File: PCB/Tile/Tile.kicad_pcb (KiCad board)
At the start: 2 copper layers, 100 x 100 mm, 95 parts, among them J1 Conn_01x04_Male, J2 Conn_01x04, J3 Conn_01x02_Male, U1 HT16K33-28SOP

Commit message: [add] Tileの回路図を作成 #3
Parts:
- removed C2: 100u, Capacitor_THT:CP_Radial_D5.0mm_P2.50mm
- removed J2: Conn_01x04, Connector:NS-Tech_Grove_1x04_P2mm_Vertical
- removed J3: Conn_01x02_Male, Connector_PinHeader_2.54mm:PinHeader_1x02_P2.54mm_Vertical
- removed JP4, JP5: Jumper_NO_Small, Jumper:SolderJumper-2_P1.3mm_Open_RoundedPad1.0x1.5mm
- removed LS1: Speaker, extsui:Speaker_UGSM23A
- removed R4, R5: 4.7k, extsui:R_1608_HandSolderingCustom
- removed TP1, TP10, TP11, TP12, TP13, TP14, TP15, TP16, TP2, TP3, TP4, TP5, TP6, TP7, TP8, TP9: TestPoint, extsui:TestPoint_Pad_2.0x2.0mm_NoSilk
- added H1: MountingHole, MountingHole:MountingHole_3.2mm_M3, F.Cu at (125.5, 185.5)
- added H2: MountingHole, MountingHole:MountingHole_3.2mm_M3, F.Cu at (125.5, 192.4)
- added H3: MountingHole, MountingHole:MountingHole_3.2mm_M3, F.Cu at (132.4, 185.5)
- added H4: MountingHole, MountingHole:MountingHole_3.2mm_M3, F.Cu at (132.4, 192.4)
- added H5: MountingHole, MountingHole:MountingHole_3.2mm_M3, F.Cu at (139.4, 185.5)
- added H6: MountingHole, MountingHole:MountingHole_3.2mm_M3, F.Cu at (139.4, 192.4)
- J1: value Conn_01x04_Male -> Conn_01x05_Female; footprint Connector_PinHeader_2.54mm:PinHeader_1x04_P2.54mm_Vertical -> Connector_PinHeader_2.54mm:PinHeader_1x05_P2.54mm_Vertical
- moved J1 8.54 mm to (115.0, 63.0), turned to 0 degrees
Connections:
- C1 pad 1: VCC -> +5V
- D9 pad 2: Net-(D25-Pad2) -> Net-(D9-Pad2)
- J1 pad 1: SCL -> +5V
- J1 pad 3: VCC -> SCL
- J1 pad 4: GND -> Net-(J1-Pad4)
- U1 pad 17: Net-(D25-Pad2) -> Net-(D9-Pad2)
- U1 pad 28: VCC -> +5V
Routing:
- net SDA: track 286.8 -> 184.0 mm, vias 9 -> 6
- net VCC: track 232.4 -> 130.2 mm, vias 9 -> 7
- net SCL: track 240.3 -> 153.1 mm, vias 11 -> 8
- net Net-(J3-Pad1): track 31.1 -> 0.00 mm
- net Net-(J3-Pad2): track 29.8 -> 0.00 mm
- net GND: track 13.1 -> 0.00 mm, vias 7 -> 4
- net Net-(JP5-Pad1): track 4.91 -> 0.00 mm
- net Net-(JP4-Pad1): track 4.91 -> 0.00 mm
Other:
- outline, holes or cut-outs redrawn
- board text added: "@ext_sui 2020.04"
- board text added: "Tile Growing v1.0"
- board text removed: "@ext_sui 2019.03"
- board text removed: "Land Growing v1.0"

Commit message: [update] TileのLED仮位置決め完了 #3
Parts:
- removed D25: LED, extsui:LED_1608_HandSolderingCustom
- removed REF1, REF2, REF3, REF4: MountingHole_3.2mm_M3, MountingHole:MountingHole_3.2mm_M3
- removed TP17, TP18, TP19, TP20, TP21, TP22, TP23, TP24, TP25, TP26, TP27, TP28, TP29, TP30, TP31, TP32, TP33, TP34, TP35, TP36, TP37, TP38, TP39, TP40, TP41, TP42, TP43, TP44, TP45, TP46, TP47, TP48: TestPoint, extsui:TestPoint_Pad_2.0x2.0mm_NoSilk
- moved H4 126.9 mm to (152.0, 67.0)
- moved H5 122.6 mm to (108.0, 67.0)
- moved H6 102.4 mm to (86.0, 105.0)
- moved H3 90.6 mm to (174.0, 105.0)
- moved D19 82.4 mm to (97.0, 91.9), turned to 60 degrees
- moved D18 78.3 mm to (102.0, 83.2), turned to 60 degrees
- moved D17 73.2 mm to (107.0, 74.5), turned to 60 degrees
- moved D20 73.1 mm to (92.0, 100.5), turned to 60 degrees
- moved D1 71.1 mm to (115.0, 140.0)
- moved D7 70.8 mm to (162.5, 118.2), turned to 60 degrees
- moved D8 69.0 mm to (167.5, 109.5), turned to 60 degrees
- moved D9 67.7 mm to (167.5, 100.5), turned to 300 degrees
- moved D10 66.7 mm to (162.5, 91.8), turned to 300 degrees
- moved D16 63.6 mm to (115.0, 70.0), turned to 0 degrees
- moved D6 63.3 mm to (157.5, 126.8), turned to 60 degrees
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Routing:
- net Net-(D1-Pad1): track 214.7 -> 0.00 mm, vias 6 -> 0
- net SDA: track 184.0 -> 0.00 mm, vias 6 -> 0
- net SCL: track 153.1 -> 0.00 mm, vias 8 -> 0
- net Net-(D17-Pad1): track 152.1 -> 0.00 mm, vias 1 -> 0
- net Net-(D23-Pad2): track 145.9 -> 0.00 mm, vias 2 -> 0
- net Net-(D22-Pad2): track 141.0 -> 0.00 mm, vias 2 -> 0
- net Net-(D24-Pad2): track 130.5 -> 0.00 mm, vias 4 -> 0
- net VCC: track 130.2 -> 0.00 mm, vias 7 -> 0
- net Net-(D21-Pad2): track 124.8 -> 0.00 mm, vias 2 -> 0
- net Net-(D25-Pad2): track 112.4 -> 0.00 mm, vias 4 -> 0
- net Net-(D20-Pad2): track 107.0 -> 0.00 mm, vias 2 -> 0
- net Net-(D19-Pad2): track 96.1 -> 0.00 mm, vias 2 -> 0
- net Net-(D18-Pad2): track 90.2 -> 0.09 mm, vias 2 -> 0
- net Net-(D10-Pad2): track 72.1 -> 0.00 mm, vias 1 -> 0
- net Net-(D12-Pad2): track 69.2 -> 0.00 mm, vias 3 -> 0
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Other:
- board size 100 x 100 mm -> 100 x 86.6 mm
- board text removed: "GND"
- board text removed: "SCL"
- board text removed: "SDA"
- board text removed: "VCC"

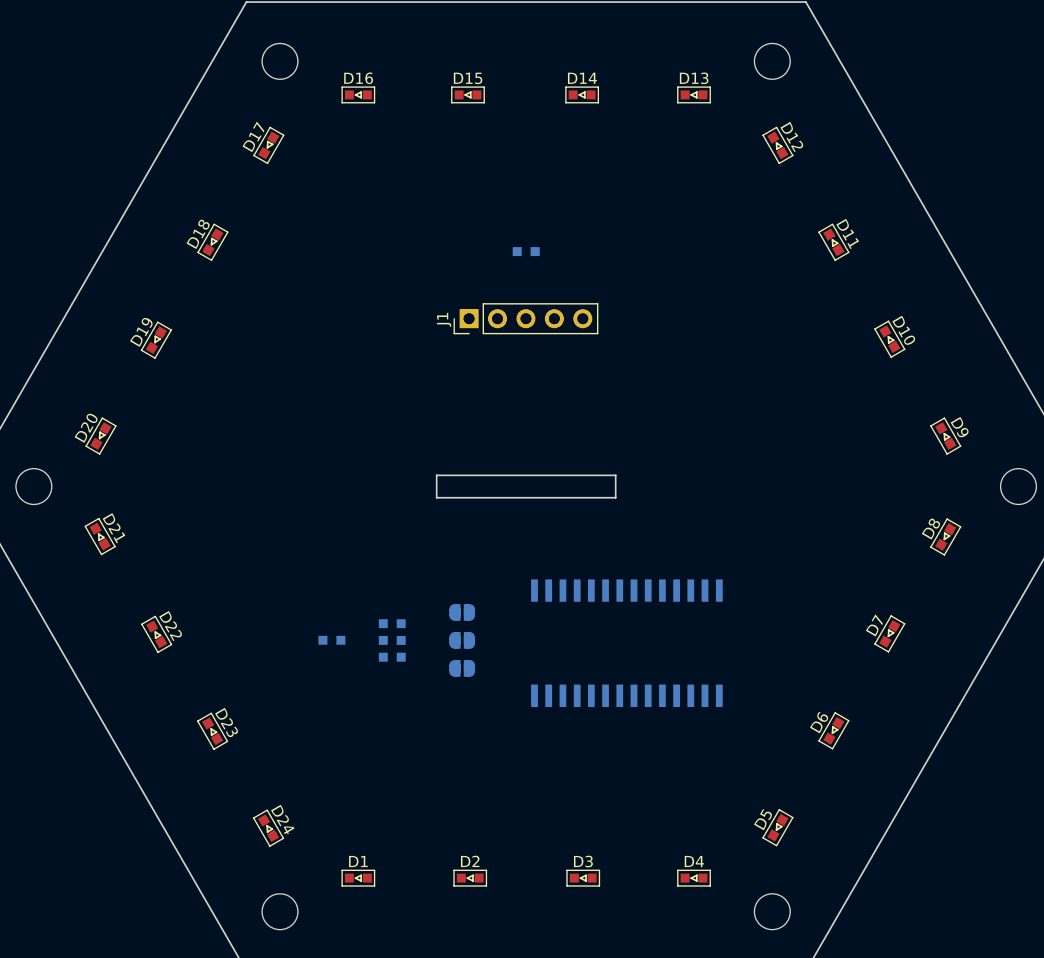
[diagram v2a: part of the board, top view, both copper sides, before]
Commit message: [update] TileのLED外周配線作成 #3
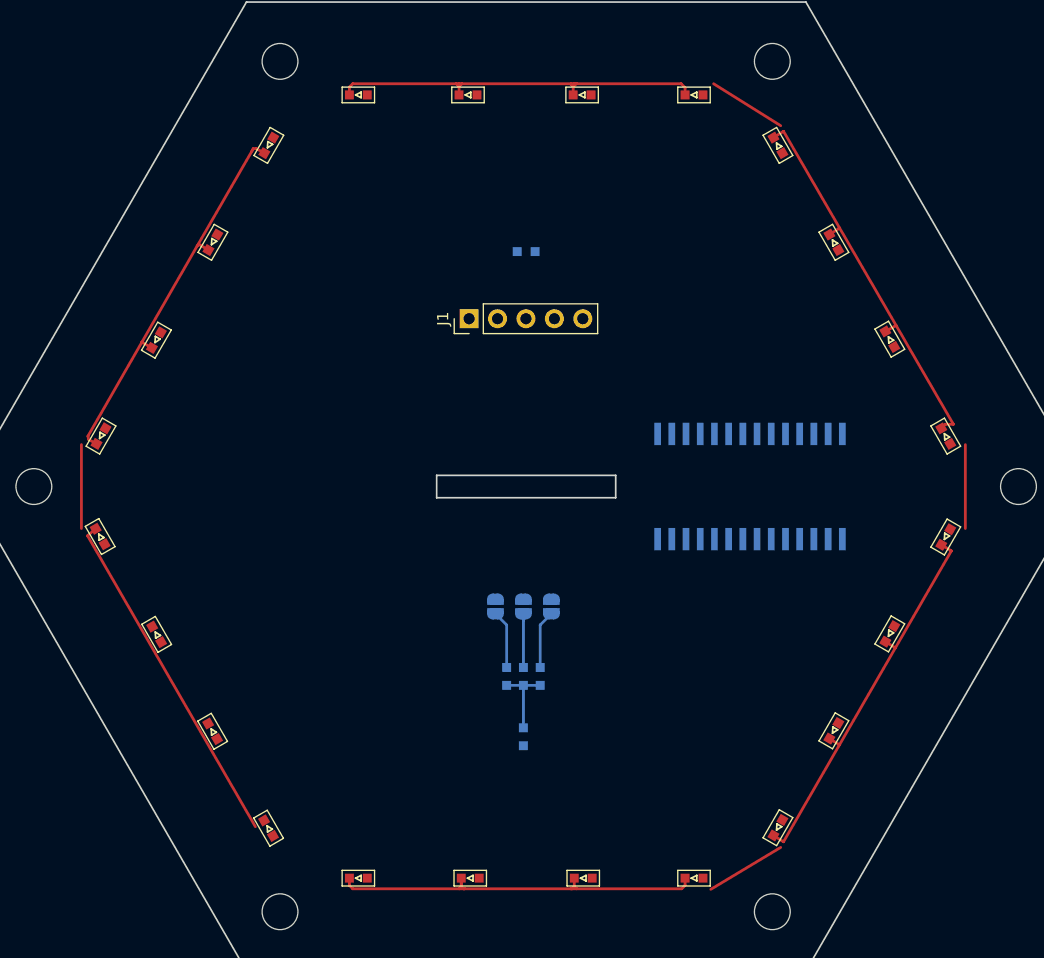
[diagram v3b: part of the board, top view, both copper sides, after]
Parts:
- moved D26 19.2 mm to (129.7, 127.4), turned to 270 degrees
- moved U1 17.8 mm to (150.0, 105.0)
- moved R1 13.3 mm to (131.3, 122.0), turned to 270 degrees
- moved R2 12.2 mm to (129.8, 122.0), turned to 270 degrees
- moved R3 11.3 mm to (128.3, 122.0), turned to 270 degrees
- moved JP1 9.71 mm to (132.3, 115.7), turned to 90 degrees
- moved JP2 6.26 mm to (129.8, 115.7), turned to 90 degrees
- moved JP3 3.02 mm to (127.3, 115.7), turned to 90 degrees
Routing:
- net Net-(D1-Pad1): track 0.00 -> 161.0 mm
- net Net-(D17-Pad1): track 0.00 -> 72.4 mm
- net Net-(D26-Pad1): track 0.01 -> 6.79 mm
- net Net-(JP3-Pad1): track 0.00 -> 5.21 mm
- net Net-(JP1-Pad1): track 0.00 -> 5.21 mm
- net Net-(JP2-Pad1): track 0.00 -> 4.80 mm

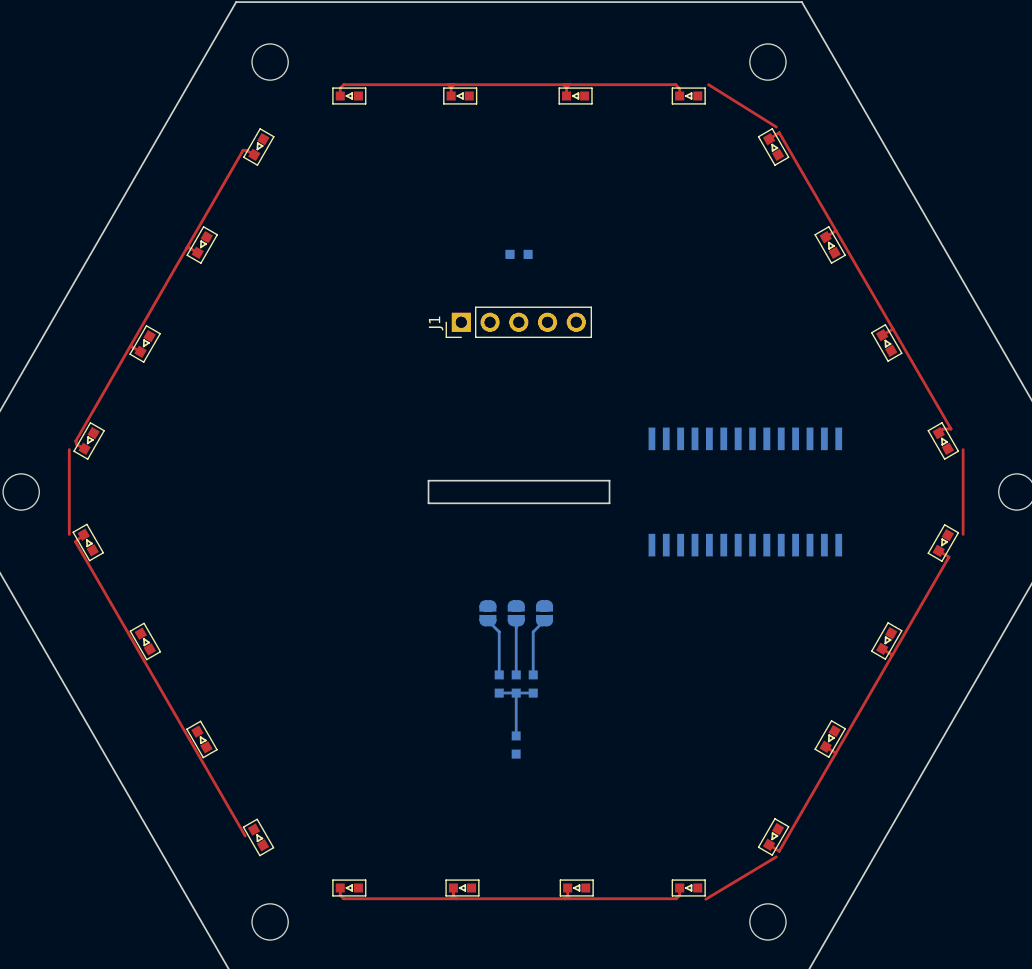
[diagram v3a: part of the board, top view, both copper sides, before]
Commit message: [update] TileのLED並び替え後の位置決め完了 #3
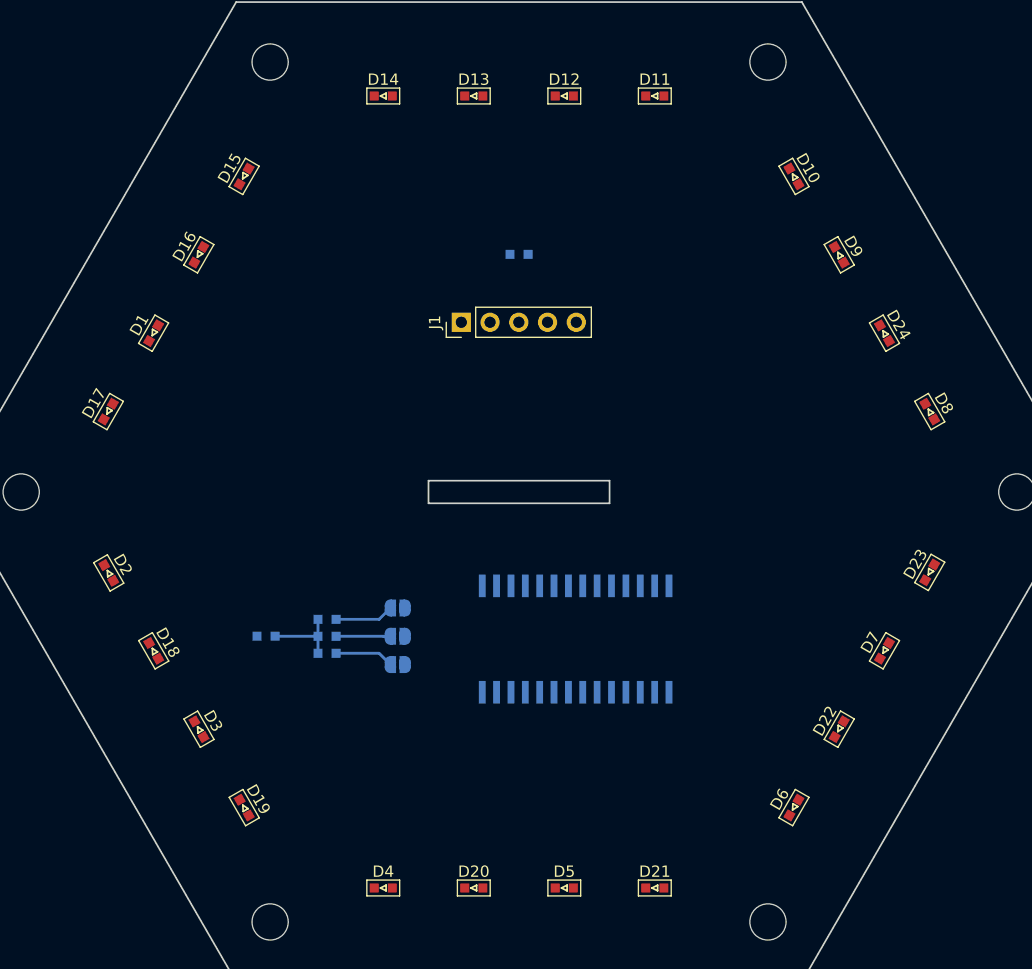
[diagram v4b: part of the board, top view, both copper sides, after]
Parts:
- moved D24 71.0 mm to (162.3, 91.0)
- moved D23 66.0 mm to (166.3, 112.1), turned to 60 degrees
- moved D22 61.8 mm to (158.3, 126.0), turned to 60 degrees
- moved D21 58.6 mm to (142.0, 140.0), turned to 0 degrees
- moved D20 52.1 mm to (126.0, 140.0), turned to 0 degrees
- moved D1 52.0 mm to (97.7, 91.0), turned to 60 degrees
- moved D19 41.9 mm to (105.7, 132.9), turned to 300 degrees
- moved D2 41.9 mm to (93.7, 112.2), turned to 300 degrees
- moved D3 36.2 mm to (101.7, 126.0), turned to 300 degrees
- moved D18 36.1 mm to (97.7, 119.0), turned to 300 degrees
- moved D4 27.0 mm to (118.0, 140.0)
- moved D17 26.9 mm to (93.7, 97.9)
- moved D26 24.1 mm to (107.6, 117.7), turned to 180 degrees
- moved D15 20.4 mm to (105.7, 77.1), turned to 60 degrees
- moved D11 20.3 mm to (142.0, 70.0), turned to 0 degrees
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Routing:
- net Net-(D1-Pad1): track 161.0 -> 0.00 mm
- net Net-(D17-Pad1): track 72.4 -> 0.00 mm

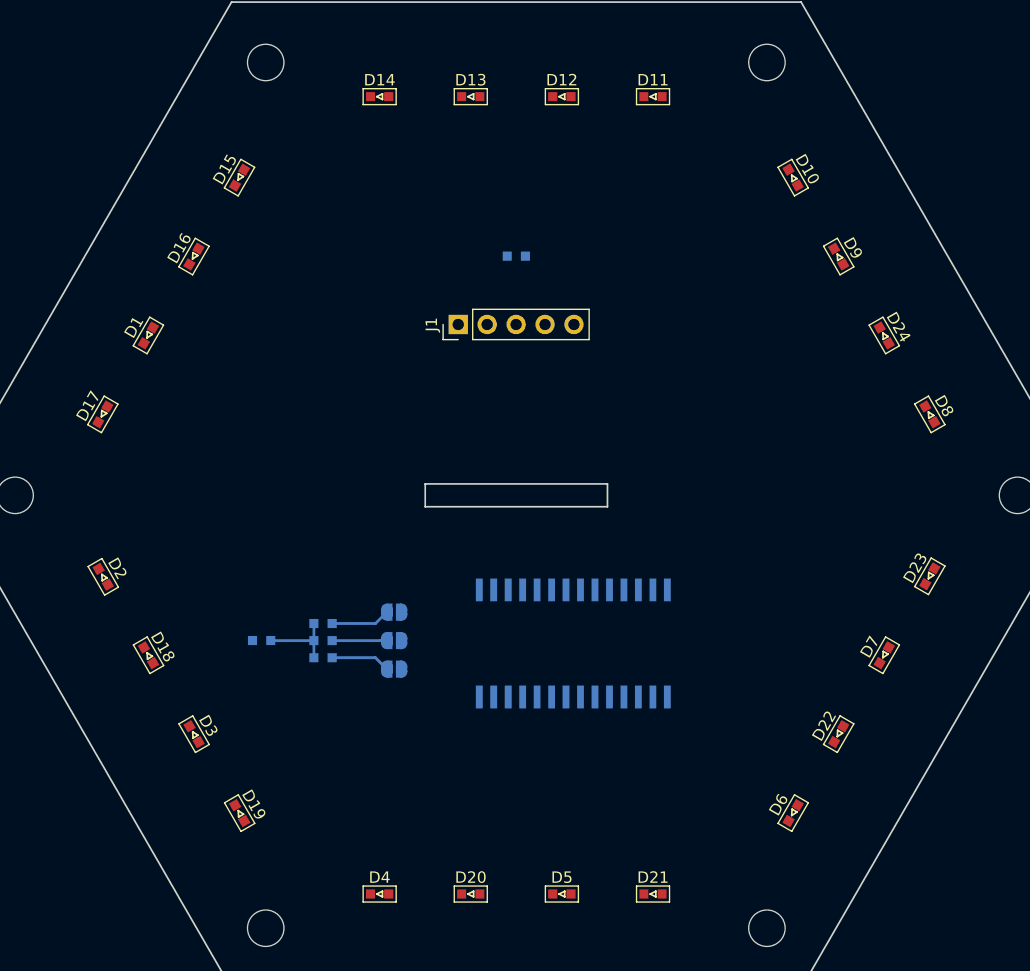
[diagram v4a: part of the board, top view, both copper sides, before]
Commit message: [update] TileのLEDの向きを配線用に最適化 #3
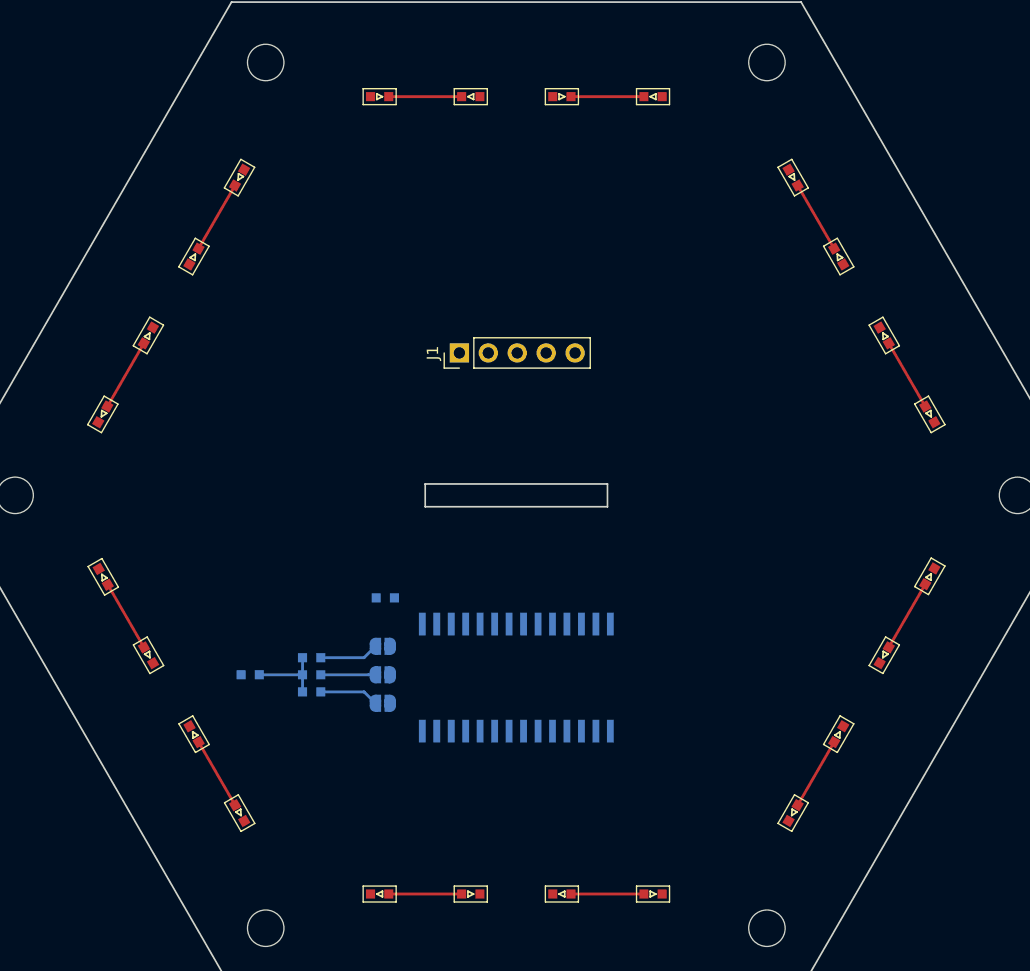
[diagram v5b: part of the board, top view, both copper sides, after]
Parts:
- moved C1 32.1 mm to (118.5, 114.0)
- moved U1 5.83 mm to (130.0, 121.0)
- moved D26 3.16 mm to (106.6, 120.7)
- moved JP1 3.16 mm to (118.3, 123.3)
- moved JP2 3.16 mm to (118.3, 120.8)
- moved JP3 3.16 mm to (118.3, 118.3)
- moved R1 3.16 mm to (112.0, 122.3)
- moved R2 3.16 mm to (112.0, 120.8)
- moved R3 3.16 mm to (112.0, 119.3)
- moved J1 2.50 mm to (125.0, 92.5)
- turned D1 to 240 degrees
- turned D10 to 120 degrees
- turned D12 to 180 degrees
- turned D14 to 180 degrees
- turned D16 to 240 degrees
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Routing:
- net Net-(D1-Pad1): track 0.00 -> 25.6 mm
- net Net-(D22-Pad2): track 0.00 -> 6.40 mm
- net Net-(D24-Pad2): track 0.00 -> 6.40 mm
- net Net-(D23-Pad2): track 0.00 -> 6.40 mm
- net Net-(D19-Pad2): track 0.00 -> 6.40 mm
- net Net-(D20-Pad2): track 0.00 -> 6.40 mm
- net Net-(D21-Pad2): track 0.00 -> 6.40 mm
- net Net-(D1-Pad2): track 0.04 -> 6.40 mm
- net Net-(D18-Pad2): track 0.09 -> 6.35 mm
